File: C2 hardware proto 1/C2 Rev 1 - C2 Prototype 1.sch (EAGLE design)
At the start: 48 parts

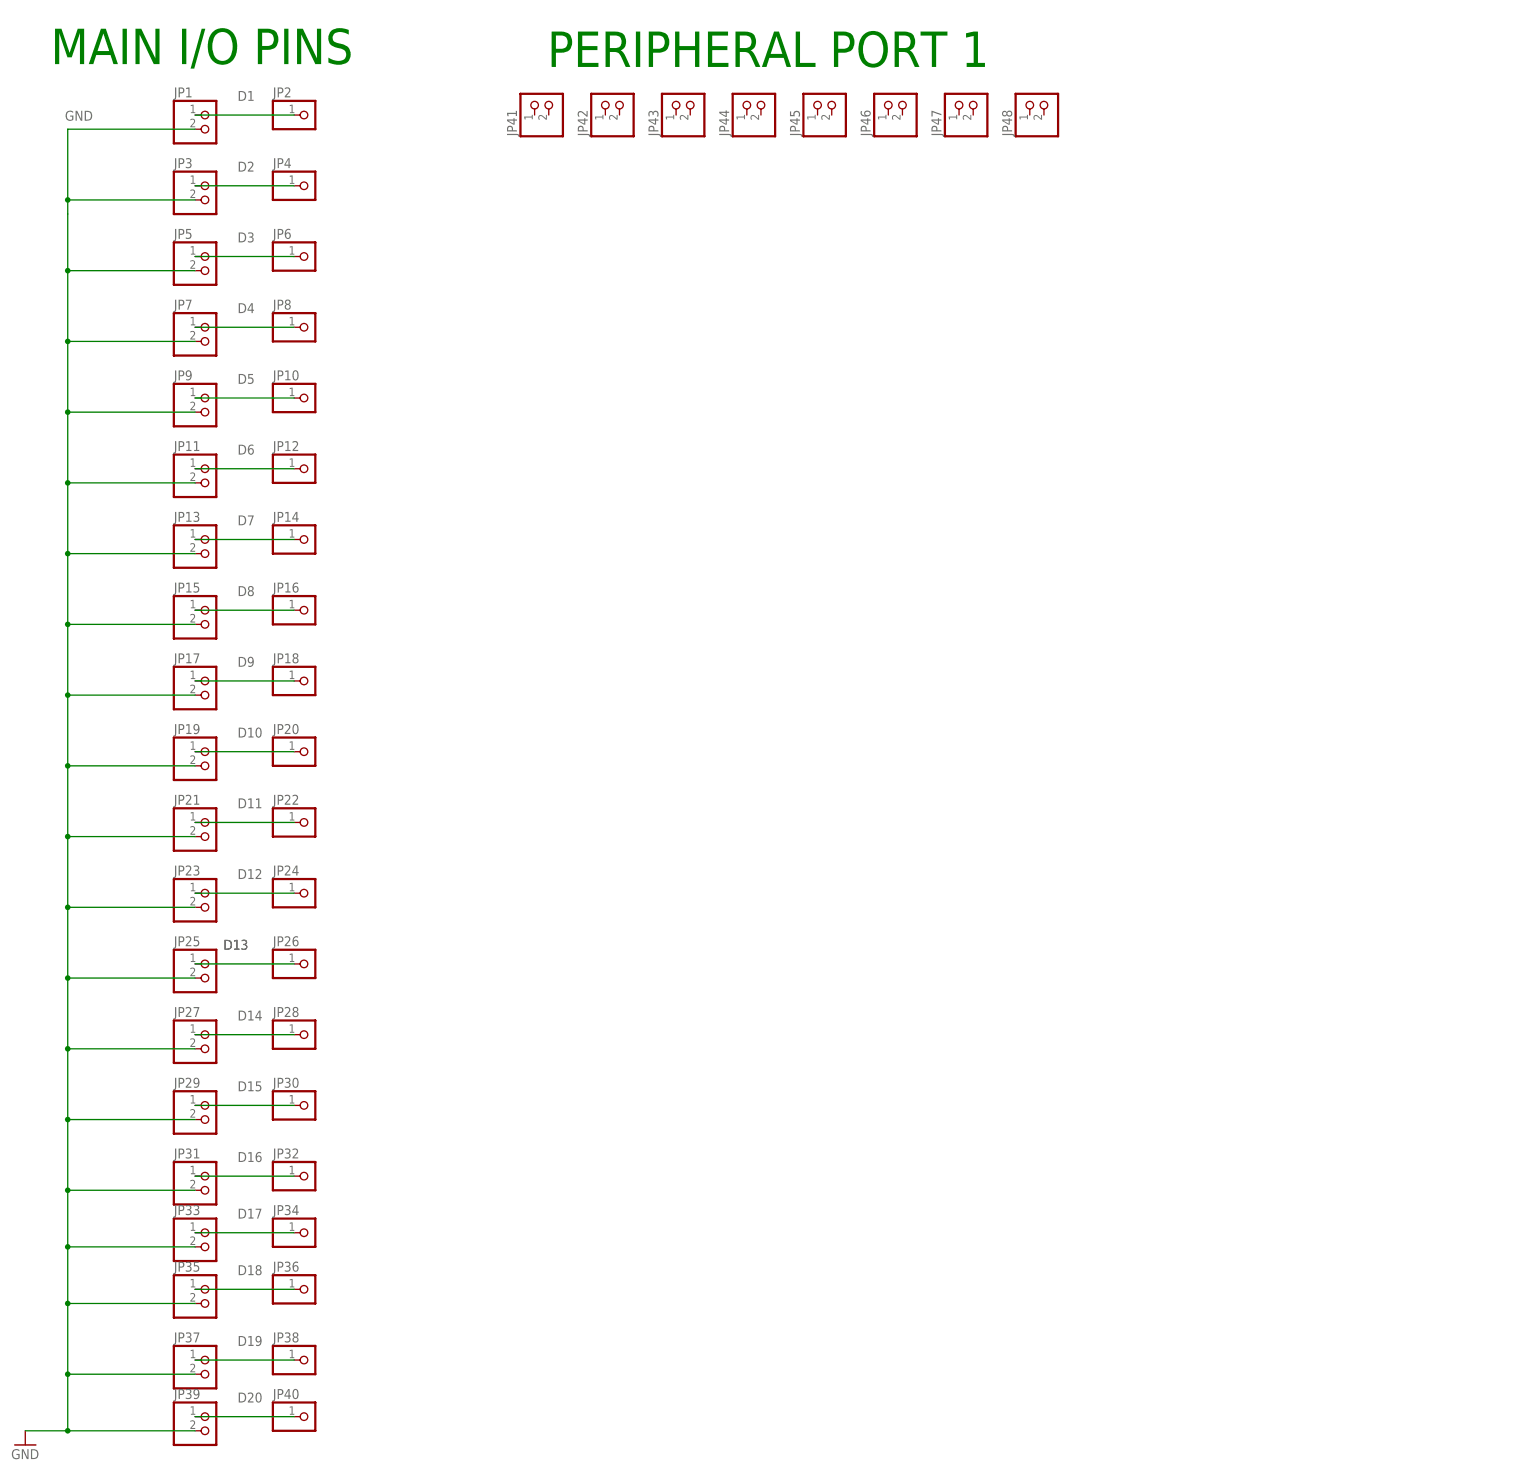
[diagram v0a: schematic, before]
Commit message: Alpha Rev 1, schem and board layed out, ready for routing
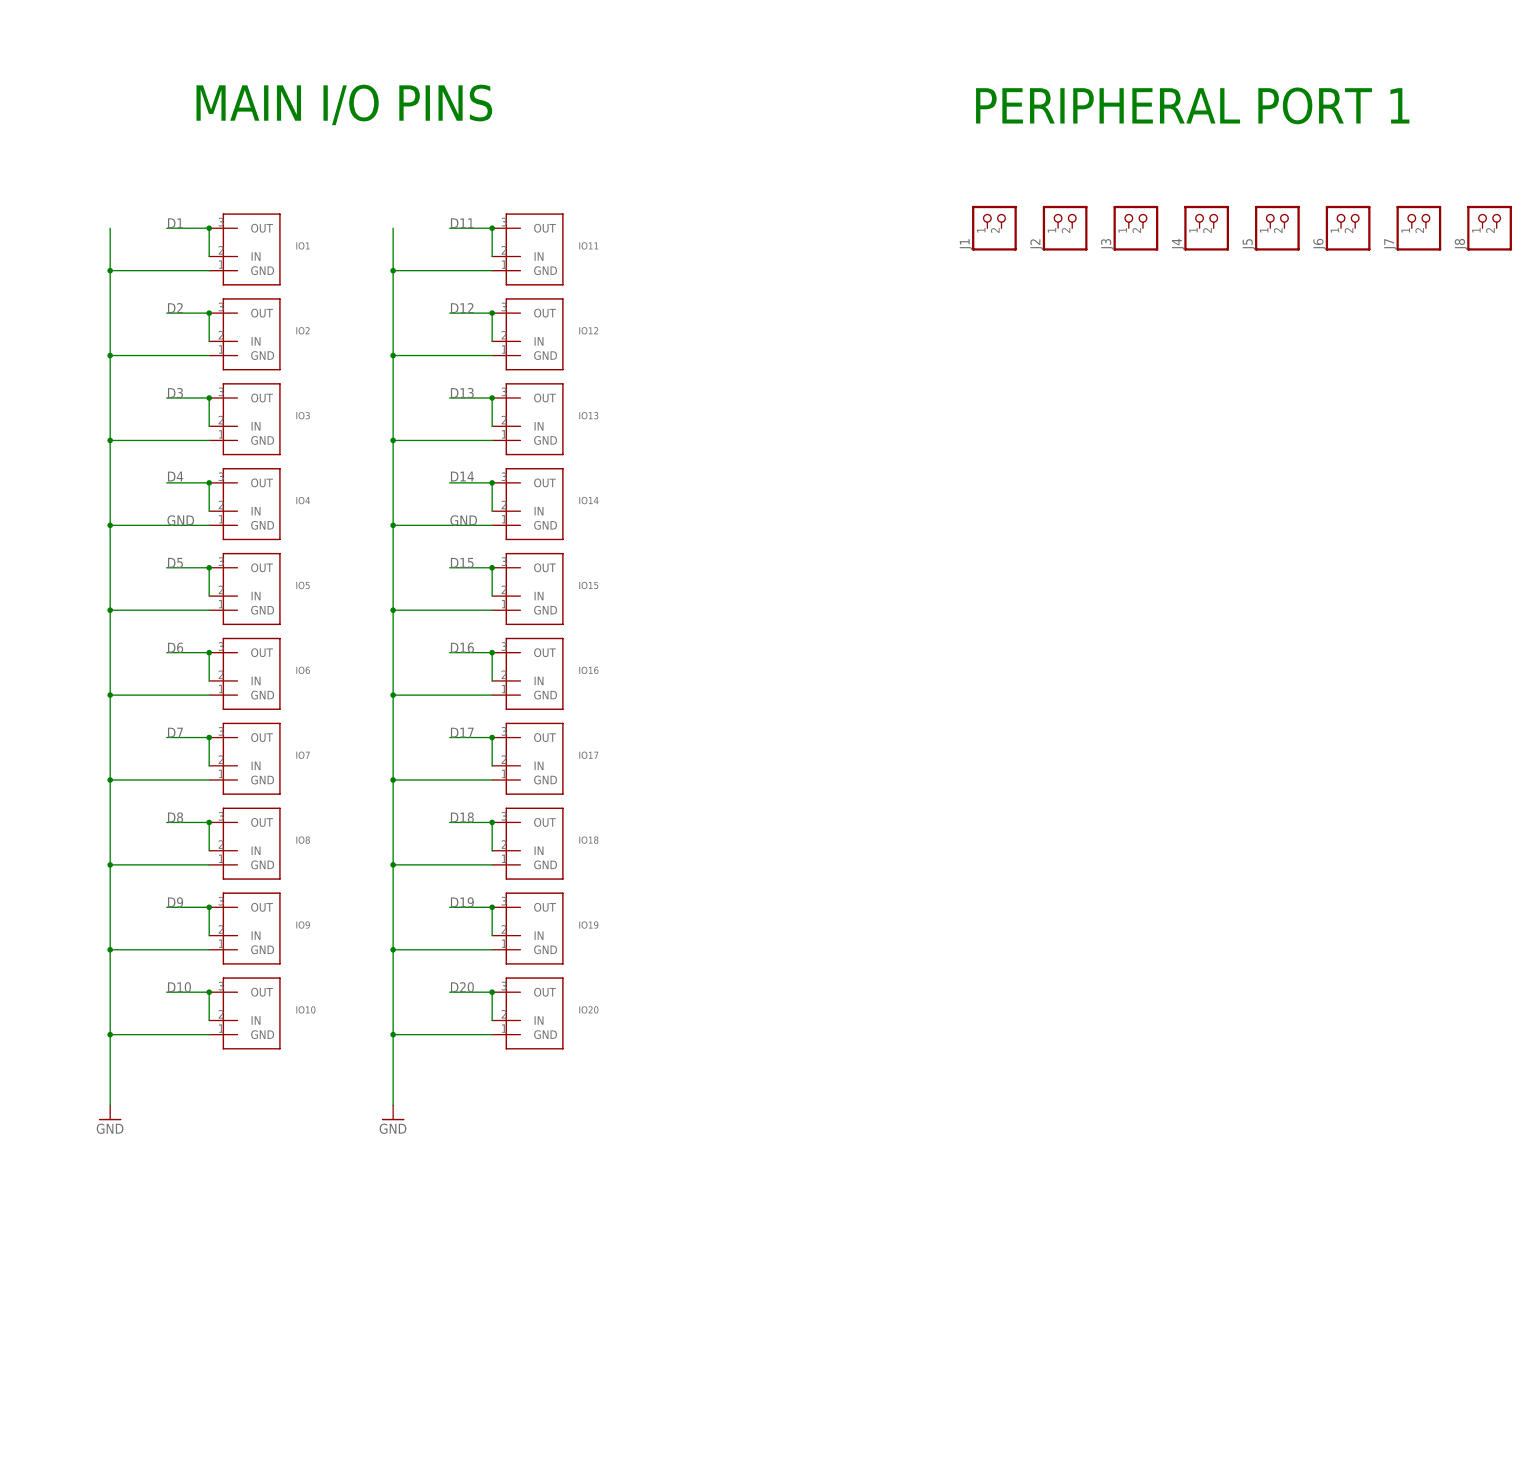
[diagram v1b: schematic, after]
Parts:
- removed JP1, JP11, JP13, JP15, JP17, JP19, JP21, JP23, JP25, JP27, JP29, JP3, JP31, JP33, JP35, JP37, JP39, JP41, JP42, JP43, JP44, JP45, JP46, JP47, JP48, JP5, JP7, JP9: (no value), pinhead:PINHD-1X2
- removed JP10, JP12, JP14, JP16, JP18, JP2, JP20, JP22, JP24, JP26, JP28, JP30, JP32, JP34, JP36, JP38, JP4, JP40, JP6, JP8: (no value), pinhead:PINHD-1X1
- added IO1, IO10, IO11, IO12, IO13, IO14, IO15, IO16, IO17, IO18, IO19, IO2, IO20, IO3, IO4, IO5, IO6, IO7, IO8, IO9: C2_IO, VanEagleLib:C2_IO
- added J1, J2, J3, J4, J5, J6, J7, J8: (no value), pinhead:PINHD-1X2
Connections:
- net D1: now also IO1.IN, IO1.OUT; no longer JP1.1, JP2.1
- net D10: now also IO10.IN, IO10.OUT; no longer JP19.1, JP20.1
- net D11: now also IO11.IN, IO11.OUT; no longer JP21.1, JP22.1
- net D12: now also IO12.IN, IO12.OUT; no longer JP23.1, JP24.1
- net D13: now also IO13.IN, IO13.OUT; no longer JP25.1, JP26.1
- net D14: now also IO14.IN, IO14.OUT; no longer JP27.1, JP28.1
- net D15: now also IO15.IN, IO15.OUT; no longer JP29.1, JP30.1
- net D16: now also IO16.IN, IO16.OUT; no longer JP31.1, JP32.1
- net D17: now also IO17.IN, IO17.OUT; no longer JP33.1, JP34.1
- net D18: now also IO18.IN, IO18.OUT; no longer JP35.1, JP36.1
- net D19: now also IO19.IN, IO19.OUT; no longer JP37.1, JP38.1
- net D2: now also IO2.IN, IO2.OUT; no longer JP3.1, JP4.1
- net D20: now also IO20.IN, IO20.OUT; no longer JP39.1, JP40.1
- net D3: now also IO3.IN, IO3.OUT; no longer JP5.1, JP6.1
- net D4: now also IO4.IN, IO4.OUT; no longer JP7.1, JP8.1
- net D5: now also IO5.IN, IO5.OUT; no longer JP10.1, JP9.1
- net D6: now also IO6.IN, IO6.OUT; no longer JP11.1, JP12.1
- net D7: now also IO7.IN, IO7.OUT; no longer JP13.1, JP14.1
- net D8: now also IO8.IN, IO8.OUT; no longer JP15.1, JP16.1
- net D9: now also IO9.IN, IO9.OUT; no longer JP17.1, JP18.1
- net GND: now also IO1.GND, IO10.GND, IO11.GND, IO12.GND, IO13.GND, IO14.GND, IO15.GND, IO16.GND, IO17.GND, IO18.GND, IO19.GND, IO2.GND, IO20.GND, IO3.GND, IO4.GND, IO5.GND, IO6.GND, IO7.GND, IO8.GND, IO9.GND; no longer JP1.2, JP11.2, JP13.2, JP15.2, JP17.2, JP19.2, JP21.2, JP23.2, JP25.2, JP27.2, JP29.2, JP3.2, JP31.2, JP33.2, JP35.2, JP37.2, JP39.2, JP5.2, JP7.2, JP9.2

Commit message: updates
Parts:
- added IC1: FEATHER-ESP32, VCO-Eagle_parts:FEATHER-ESP32
- added JP1, JP10, JP11, JP12, JP13, JP14, JP15, JP16, JP17, JP18, JP19, JP2, JP20, JP21, JP22, JP23, JP24, JP25, JP26, JP27, JP28, JP3, JP4, JP5, JP6, JP7, JP8, JP9: PROTO_VIA_COMPACT, VanEagleLib:PROTO_VIA_COMPACT
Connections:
- removed net GND: IO1.GND, IO10.GND, IO11.GND, IO12.GND, IO13.GND, IO14.GND, IO15.GND, IO16.GND, IO17.GND, IO18.GND, IO19.GND, IO2.GND, IO20.GND, IO3.GND, IO4.GND, IO5.GND, IO6.GND, IO7.GND, IO8.GND, IO9.GND
- new net COM: IO1.COM, IO1.SW1, IO10.COM, IO10.SW1, IO11.COM, IO11.SW1, IO12.COM, IO12.SW1, IO13.COM, IO13.SW1, IO14.COM, IO14.SW1, IO15.COM, IO15.SW1, IO16.COM, IO16.SW1, IO17.COM, IO17.SW1, IO18.COM, IO18.SW1, IO19.COM, IO19.SW1, IO2.COM, IO2.SW1, IO20.COM, IO20.SW1, IO3.COM, IO3.SW1, IO4.COM, IO4.SW1, IO5.COM, IO5.SW1, IO6.COM, IO6.SW1, IO7.COM, IO7.SW1, IO8.COM, IO8.SW1, IO9.COM, IO9.SW1
- new net N$1: IC1.RST, JP28.1
- new net N$10: IC1.A5, JP19.1
- new net N$11: IC1.SCK, JP18.1
- new net N$12: IC1.MOSI, JP17.1
- new net N$13: IC1.MISO, JP16.1
- new net N$14: IC1.IO16, JP15.1
- new net N$15: IC1.IO17, JP14.1
- new net N$16: IC1.IO21, JP13.1
- new net N$17: IC1.SDA, JP12.1
- new net N$18: IC1.SCL, JP11.1
- new net N$19: IC1.IO14, JP10.1
- new net N$2: IC1.3.3V, JP27.1
- new net N$20: IC1.IO32, JP9.1
- new net N$21: IC1.IO15, JP8.1
- new net N$22: IC1.IO33, JP7.1
- new net N$23: IC1.IO27, JP6.1
- new net N$24: IC1.IO12, JP5.1
- new net N$25: IC1.IO13, JP4.1
- new net N$26: IC1.USB, JP3.1
- new net N$27: IC1.EN, JP2.1
- new net N$28: IC1.BAT, JP1.1
- new net N$3: IC1.NC, JP26.1
- new net N$4: IC1.GND, JP25.1
- new net N$5: IC1.A0, JP24.1
- new net N$6: IC1.A1, JP23.1
- new net N$7: IC1.A2, JP22.1
- new net N$8: IC1.A3, JP21.1
- new net N$9: IC1.A4, JP20.1
- net D1: now also IO1.SW2; no longer IO1.IN
- net D10: now also IO10.SW2; no longer IO10.IN
- net D11: now also IO11.SW2; no longer IO11.IN
- net D12: now also IO12.SW2; no longer IO12.IN
- net D13: now also IO13.SW2; no longer IO13.IN
- net D14: now also IO14.SW2; no longer IO14.IN
- net D15: now also IO15.SW2; no longer IO15.IN
- net D16: now also IO16.SW2; no longer IO16.IN
- net D17: now also IO17.SW2; no longer IO17.IN
- net D18: now also IO18.SW2; no longer IO18.IN
- net D19: now also IO19.SW2; no longer IO19.IN
- net D2: now also IO2.SW2; no longer IO2.IN
- net D20: now also IO20.SW2; no longer IO20.IN
- net D3: now also IO3.SW2; no longer IO3.IN
- net D4: now also IO4.SW2; no longer IO4.IN
- net D5: now also IO5.SW2; no longer IO5.IN
- net D6: now also IO6.SW2; no longer IO6.IN
- net D7: now also IO7.SW2; no longer IO7.IN
- net D8: now also IO8.SW2; no longer IO8.IN
- net D9: now also IO9.SW2; no longer IO9.IN
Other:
- moved on the sheet: J1, J2, J3, J4, J5, J6, J7, J8
